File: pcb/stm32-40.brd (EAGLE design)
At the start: 69.8 x 57.1 mm, 97 parts, among them IC1 STM32F103RBT6, IC2 CAT24M01WI-GT3, IC3 MAX487-S, IC4 AMIS30663CANG2G, Q1 32768Hz, Q2 8MHz, Q3 MMBT2222, SW1 KSS-2EG4430, SW2 KSS-2EG4430, SW3 KSS-2EG4430, SW4 KSS-2EG4430, SW5 KSS-2EG4430, X1 MCV3, X2 MCV3

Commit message: ...
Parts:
- added R45, R46: 200, rc-master-smd:R0603
- R42: value 4.7K -> 200
- moved Q3 31.2 mm to (48.3, 60.3)
- moved R42 20.3 mm to (17.8, 51.4), turned to 270 degrees
- moved R44 18.2 mm to (54.6, 59.7)
- moved LCD1 1.42 mm to (39.4, 37.5)
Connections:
- removed net BL: R44.2
- net !LCD_CS: now also R46.2
- net !RESET: no longer R42.2
- net GND: no longer R42.1
- net LCD_CLK: now also R45.2
- net LCD_DATA: now also R42.2
- net PA1: now also R46.1
- net PA2: now also R42.1
- net PA4: now also R45.1
- net PD2: now also R44.2
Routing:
- net TIM3_CH4: track 46.4 -> 51.4 mm
- net TIM3_CH2: track 54.5 -> 59.4 mm
- net TIM3_CH3: track 49.1 -> 53.7 mm
- net N$44: track 12.3 -> 16.4 mm, vias 2 -> 0
- net TIM3_CH1: track 58.5 -> 62.5 mm

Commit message: pcb...
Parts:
- moved R43 53.1 mm to (40.6, 14.6), turned to 90 degrees
- moved Q3 49.6 mm to (46.4, 10.8), turned to 90 degrees
- moved R44 43.8 mm to (54.0, 15.9), turned to 90 degrees
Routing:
- net !LCD_CS: track 0.00 -> 61.5 mm
- net LCD_DATA: track 0.00 -> 60.9 mm, vias 0 -> 2
- net LCD_CLK: track 0.00 -> 59.0 mm, vias 0 -> 2
- net PD2: track 41.7 -> 79.7 mm
- net PC13: track 9.00 -> 46.0 mm
- net +3V3: track 111.0 -> 131.6 mm
- net N$32: track 0.00 -> 11.5 mm
- net N$31: track 0.00 -> 5.23 mm
- net N$29: track 0.00 -> 4.05 mm
- net SWDIO: track 46.9 -> 44.1 mm
- net BOOT0: track 48.9 -> 46.2 mm
- net SWCLK: track 49.9 -> 47.2 mm
- net !RESET: track 70.3 -> 67.7 mm
- net GND: vias 25 -> 31

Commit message: final route
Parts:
- moved G1 70.8 mm to (14.0, 15.2), turned to 270 degrees
- moved C13 55.1 mm to (39.1, 14.6), turned to 270 degrees
- moved R41 24.4 mm to (11.4, 48.3), turned to 180 degrees
- moved R2 16.6 mm to (19.1, 26.0), flipped to the top
- moved R5 3.18 mm to (5.08, 22.9)
- moved C14 2.54 mm to (8.26, 9.53)
- moved U1 2.54 mm to (8.26, 15.9)
- moved R1 1.42 mm to (1.91, 13.3), turned to 270 degrees
- moved R25 1.42 mm to (54.0, 20.3)
- moved R44 1.27 mm to (52.7, 15.9)
- moved SW5 1.27 mm to (15.9, 29.8)
- moved C19 1.27 mm to (47.0, 33.7)
- moved SW4 0.64 mm to (15.9, 37.5)
- moved C1 0.64 mm to (37.5, 18.4)
- moved C2 0.64 mm to (39.1, 18.4)
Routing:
- net +5V: track 23.7 -> 136.6 mm, vias 0 -> 4
- net +3V3: track 131.6 -> 183.5 mm, vias 5 -> 8
- net VBAT: track 5.78 -> 30.8 mm, vias 0 -> 3
- net !RESET: track 67.7 -> 89.0 mm, vias 3 -> 4
- net N$30: track 9.38 -> 29.0 mm, vias 1 -> 0
- net PC13: track 46.0 -> 64.6 mm
- net !LCD_CS: track 61.5 -> 67.9 mm
- net PA4: track 41.8 -> 46.9 mm
- net BOOT1: track 4.60 -> 9.26 mm, vias 0 -> 1
- net N$2: track 17.1 -> 20.6 mm, vias 1 -> 3
- net N$44: track 16.4 -> 13.3 mm, vias 0 -> 2
- net PA2: track 42.7 -> 45.3 mm
- net PA1: track 45.0 -> 47.4 mm
- net RXD1: track 45.9 -> 43.7 mm
- net LCD_CLK: track 59.0 -> 60.9 mm
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
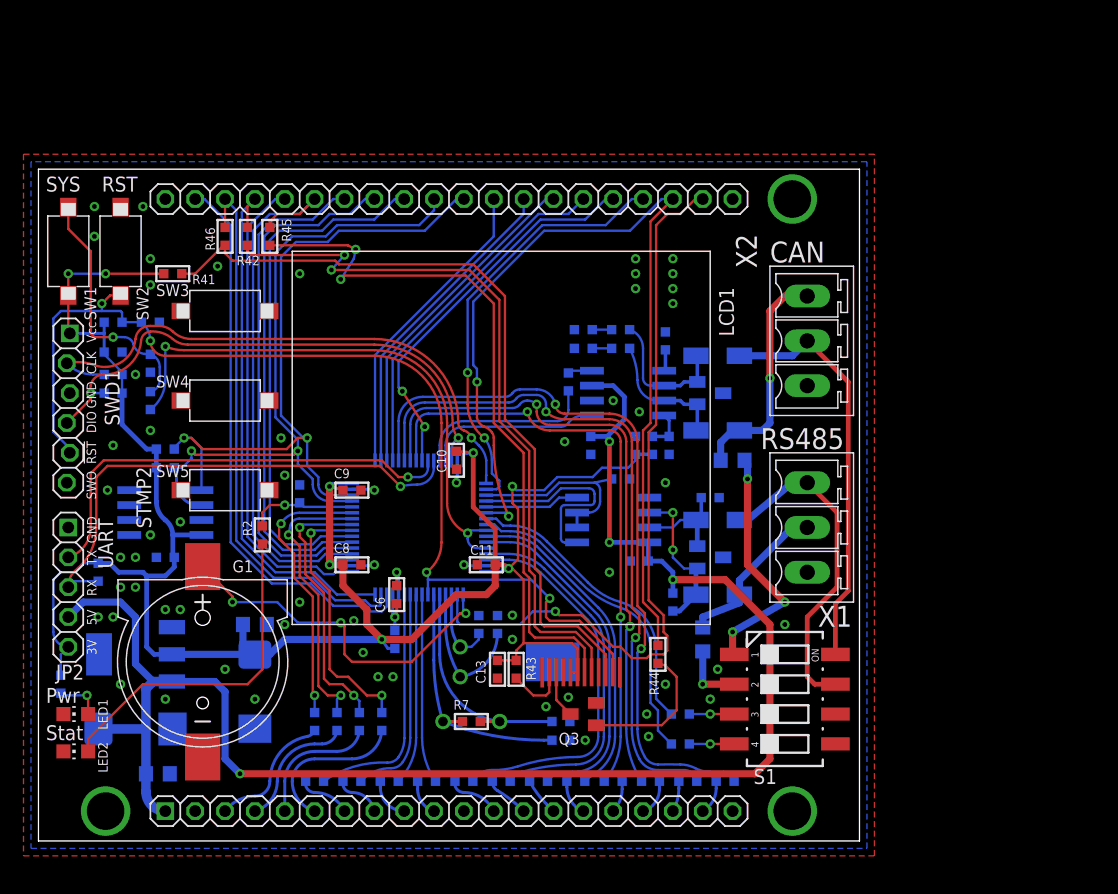
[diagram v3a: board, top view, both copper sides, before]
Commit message: 40 pin mesonine module done. Need check sch and pcb
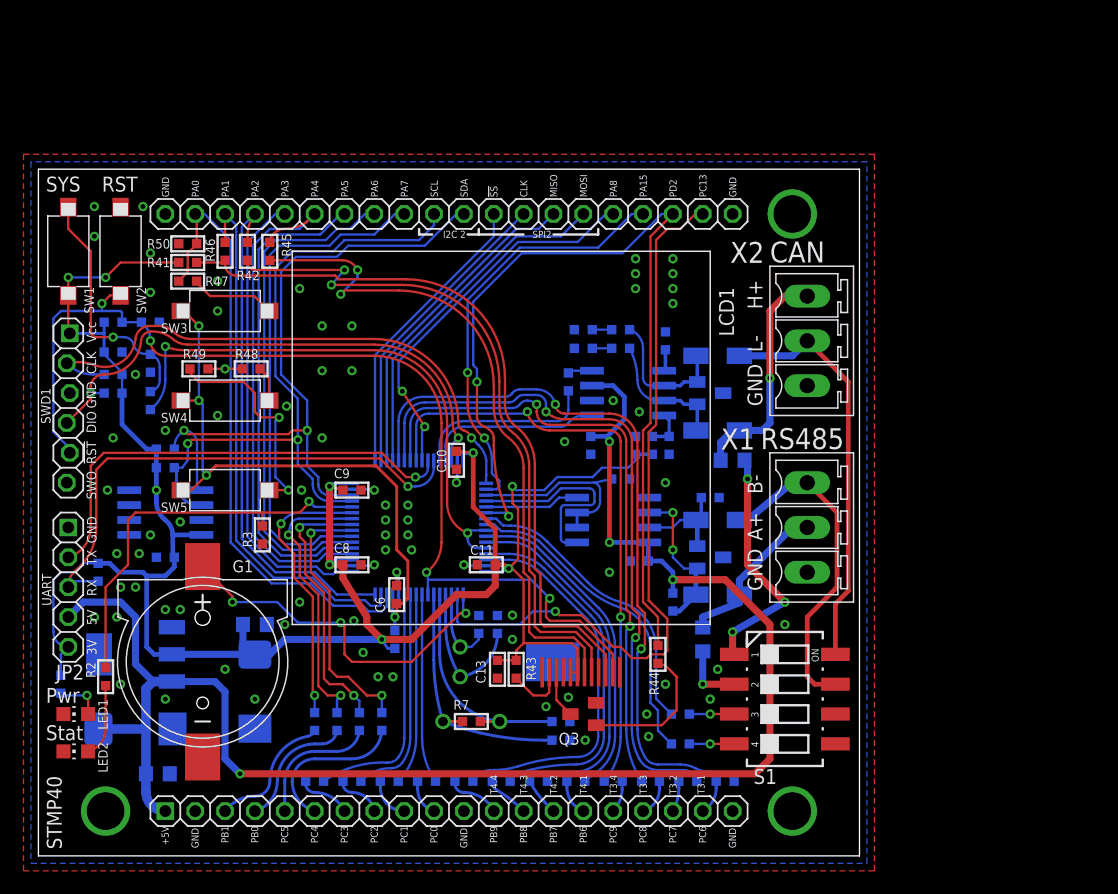
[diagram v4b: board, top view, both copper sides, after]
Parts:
- added R47, R50: 1K, rc-master-smd:R0603
- added R48: 2K, rc-master-smd:R0603
- added R49: 3.9K, rc-master-smd:R0603
- moved R2 18.0 mm to (5.71, 14.0)
- moved R3 4.72 mm to (19.1, 26.0), flipped to the top, turned to 270 degrees
- moved R41 1.59 mm to (12.7, 49.2)
- moved R42 1.27 mm to (17.8, 50.2)
- moved R45 1.27 mm to (19.7, 50.2)
- moved R46 1.27 mm to (15.9, 50.2)
- renumbered STMP2 to STMP40
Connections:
- new net N$33: R47.1, SW3.2
- new net N$34: R48.1, SW4.2
- new net N$35: R49.1, SW5.2
- net GND: now also R50.1; no longer SW3.1, SW4.1, SW5.1
- net PA0: now also R47.2, R48.2, R49.2, R50.2
- net VDDA: now also SW3.1, SW4.1, SW5.1
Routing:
- net VDDA: track 4.32 -> 51.8 mm, vias 1 -> 4
- net BOOT1: track 9.26 -> 34.5 mm
- net N$30: track 29.0 -> 6.10 mm
- net N$35: track 0.00 -> 18.9 mm, vias 0 -> 2
- net PA0: track 47.8 -> 56.3 mm, vias 0 -> 1
- net !LCD_CS: track 67.9 -> 60.6 mm
- net N$33: track 0.00 -> 7.29 mm
- net LCD_DATA: track 62.6 -> 57.4 mm
- net LCD_CLK: track 60.9 -> 55.9 mm
- net N$34: track 0.00 -> 3.02 mm
- net PA4: track 46.9 -> 45.1 mm
- net PD2: track 81.3 -> 79.5 mm
- net PA2: track 45.3 -> 43.9 mm
- net PA5: track 43.0 -> 41.7 mm
- net SPI2_SCLK: track 27.3 -> 26.0 mm
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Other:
- board size 69.8 x 57.1 mm -> 69.8 x 58.4 mm
- board text added: "!SS"
- board text added: "+5V"
- board text added: "A+"
- board text added: "B-"
- board text added: "CLK"
- board text added: "GND"
- board text added: "H+"
- board text added: "I2C 2"
- board text added: "L-"
- board text added: "MISO"
- board text added: "MOSI"
- board text added: "PA0"
- board text added: "PA1"
- board text added: "PA15"
- board text added: "PA2"
- board text added: "PA3"
- board text added: "PA4"
- board text added: "PA5"
- board text added: "PA6"
- board text added: "PA7"
- board text added: "PA8"
- board text added: "PB0"
- board text added: "PB1"
- board text added: "PB6"
- board text added: "PB7"
- board text added: "PB8"
- board text added: "PB9"
- board text added: "PC0"
- board text added: "PC1"
- board text added: "PC13"
- board text added: "PC2"
- board text added: "PC3"
- board text added: "PC4"
- board text added: "PC5"
- board text added: "PC6"
- board text added: "PC7"
- board text added: "PC8"
- board text added: "PC9"
- board text added: "PD2"
- board text added: "SCL"
- board text added: "SDA"
- board text added: "SPI2"
- board text added: "T3.1"
- board text added: "T3.2"
- board text added: "T3.3"
- board text added: "T3.4"
- board text added: "T4.1"
- board text added: "T4.2"
- board text added: "T4.3"
- board text added: "T4.4"

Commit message: stm32-40 ready to production PCB. some changes in platform
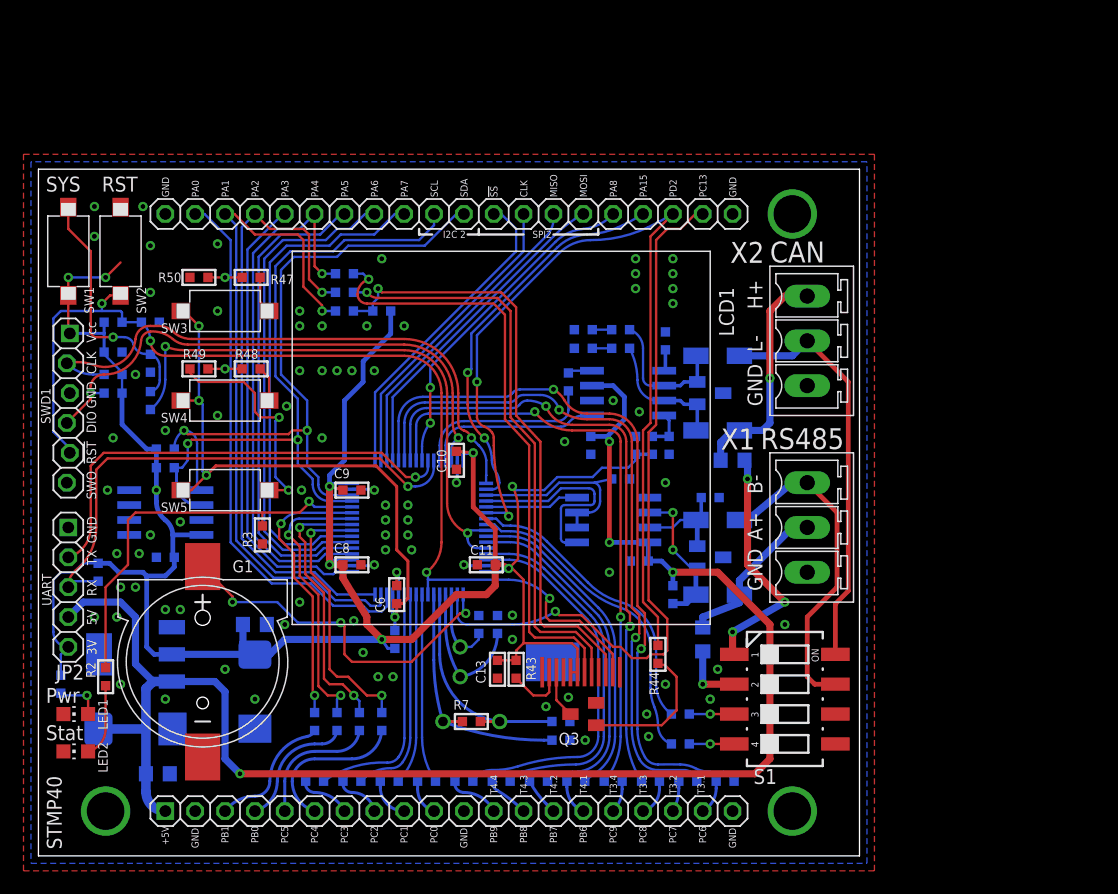
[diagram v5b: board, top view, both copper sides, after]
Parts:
- added U$1: LOGO, logo:TT_LOGO
- moved R41 17.0 mm to (29.2, 45.1), flipped to the bottom
- moved R46 11.4 mm to (26.0, 45.1), flipped to the bottom, turned to 180 degrees
- moved R42 8.96 mm to (26.0, 46.7), flipped to the bottom, turned to 180 degrees
- moved R45 6.63 mm to (26.0, 48.3), flipped to the bottom, turned to 180 degrees
- moved R47 5.41 mm to (18.1, 47.9)
- moved R50 3.01 mm to (13.7, 47.9)
- moved R25 0.63 mm to (54.0, 21.0)
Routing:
- net PA1: track 46.1 -> 59.1 mm, vias 0 -> 1
- net +3V3: track 184.7 -> 196.7 mm
- net PA2: track 43.9 -> 53.2 mm, vias 0 -> 1
- net !LCD_CS: track 60.6 -> 52.0 mm, vias 0 -> 1
- net LCD_DATA: track 57.4 -> 49.3 mm, vias 2 -> 1
- net LCD_CLK: track 55.9 -> 51.5 mm, vias 2 -> 1
- net N$33: track 7.29 -> 3.17 mm
- net PA8: track 32.6 -> 28.6 mm
- net PA0: track 56.3 -> 53.4 mm, vias 1 -> 2
- net PD2: track 79.5 -> 76.6 mm
- net PA15: track 35.8 -> 32.9 mm
- net SPI2_MOSI: track 29.9 -> 27.9 mm
- net SPI2_NSS: track 25.2 -> 27.1 mm
- net PA4: track 45.1 -> 46.7 mm, vias 0 -> 1
- net BOOT0: track 46.2 -> 47.7 mm
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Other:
- board text added: "STM32 stamp module Rev.A.14"
- board text added: "tuxotronic.org"

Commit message: some pcb fixes
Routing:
- net +3V3: track 196.7 -> 183.6 mm, vias 9 -> 7
- net !LCD_CS: track 52.0 -> 48.3 mm
- net LCD_DATA: track 49.3 -> 45.7 mm
- net LCD_CLK: track 51.5 -> 48.1 mm
- net BOOT1: track 34.5 -> 32.9 mm
- net TXD1: track 39.4 -> 38.2 mm
- net N$35: track 18.9 -> 17.8 mm
- net PA2: track 53.2 -> 52.2 mm
- net RXD1: track 44.7 -> 43.6 mm
- net N$32: track 12.2 -> 11.2 mm
- net PD2: track 76.6 -> 75.7 mm
- net PA1: track 59.1 -> 58.3 mm
- net PB0: track 24.0 -> 23.4 mm
- net PC4: track 22.7 -> 22.1 mm
- net GND: vias 82 -> 91

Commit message: little button fix
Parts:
- added R51: 330, rc-master-smd:R0603
- C1, C2: value 10pF -> 0.1
- C14, C16: value 100uF/6V3 -> 0.1; device rc-master-smd:SMC_D -> rc-master-smd:C0603
- C17: device rc-master-smd:C0805 -> rc-master-smd:C0603
- C19, C20: value 0.1 -> 560pF
- C21: value 0.1 -> 100uF/6V3; device rc-master-smd:C0603 -> rc-master-smd:SMC_D
- C22: value 560pF -> 0.1; device rc-master-smd:C0603 -> rc-master-smd:C0805
- C23: value 560pF -> 100uF/6V3; device rc-master-smd:C0603 -> rc-master-smd:SMC_D
- C3: value 22pF -> 0.1
- C4: value 22pF -> 10pF
- C5: value 0.1 -> 10pF
- C6, C7: value 0.1 -> 22pF
- IC1: value STM32F103RBT6 -> CAT24M01WI-GT3; device stm32:TQFP64 -> stm32-by-pb:SO08
- IC2: value CAT24M01WI-GT3 -> STM32F103RBT6; device stm32-by-pb:SO08 -> stm32:TQFP64
- IC3: value MAX487-S -> AMIS30663CANG2G; device rs232-rs485:SO08 -> interfaces:SO08
- IC4: value AMIS30663CANG2G -> MAX487-S; device interfaces:SO08 -> rs232-rs485:SO08
- R1, R2: value 220 -> 10K
- R10: value 10K -> 2.2K
- R11, R41: value 4.7K -> 10K
- R12: value 4.7K -> 1K
- R13, R22: value 10 -> 2K
- R14: value 10 -> 3.9K
- R15: value 10 -> 1M
- R16: value 10 -> 1K
- R17, R18, R19: value 10 -> 200
- R20: value 10 -> 4.7K
- R23: value 10 -> 10K
- R24: value 10 -> 100
- R25, R27: value 560 -> 10
- R26: value 10K -> 10
- R28, R30: value 120 -> 10; device rc-master-smd:R0805 -> rc-master-smd:R0603
- R29, R31: value 330 -> 10
- R3, R4: value 10K -> 4.7K
- R32: value 0 -> 10
- R33, R34, R35: value 100 -> 10
- R36: value NC -> 10
- R42: value 200 -> 0
- R43: value 10 -> NC
- R44: value 2K -> 560
- R45: value 200 -> 100
- R46: value 200 -> 560
- R47: value 1K -> 100
- R48: value 2K -> 120; device rc-master-smd:R0603 -> rc-master-smd:R0805
- R49: value 3.9K -> 120; device rc-master-smd:R0603 -> rc-master-smd:R0805
- R5: value 10K -> 220
- R50: value 1K -> 330
- R6: value 2.2K -> 220
- R7: value 1M -> 10K
- moved C21 55.9 mm to (8.26, 9.53), turned to 180 degrees
- moved R16 55.5 mm to (13.7, 47.9), flipped to the top
- moved R50 55.3 mm to (54.6, 10.8), flipped to the bottom
- moved R14 54.4 mm to (13.7, 40.2), flipped to the top, turned to 0 degrees
- moved R13 53.4 mm to (18.1, 40.2), flipped to the top
- moved C7 50.4 mm to (44.5, 8.57)
- moved C17 49.3 mm to (50.8, 33.7), turned to 90 degrees
- moved C3 48.7 mm to (9.53, 44.1)
- moved R18 46.2 mm to (26.0, 48.3)
- moved R49 46.1 mm to (59.1, 32.4), flipped to the bottom, turned to 180 degrees
- moved R17 46.0 mm to (26.0, 46.7)
- moved C14 45.2 mm to (51.1, 23.8), turned to 0 degrees
- moved R48 44.8 mm to (56.5, 17.1), flipped to the bottom, turned to 270 degrees
- moved R35 44.7 mm to (26.7, 5.08)
- moved R19 42.2 mm to (26.0, 45.1)
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- renumbered JP2 to JP1, STMP40 to STMP1
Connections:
- new net PB5: IC2.57, R7.1
- net !LCD_CS: now also R19.2, R20.1; no longer R41.1, R46.2
- net !RESET: now also C3.1, IC2.7, R11.1, SW1.2; no longer C5.1, IC1.7, R8.1, SW2.2
- net +3V3: now also C1.1, C17.1, C2.1, C22.1, C23.+, IC1.8, IC2.19, IC2.32, IC2.48, IC2.64, R1.2, R2.2, R20.2, R21.2, R23.2, R3.2, R4.2, R42.1, R5.1, SW2.2; no longer C11.1, C15.1, C16.+, C20.1, C7.1, IC1.19, IC1.32, IC1.48, IC1.64, IC2.8, R1.1, R10.2, R12.2, R32.1, R41.2, R43.2, R5.2, R8.2, R9.2, SW1.2
- net +5V: now also C14.1, C15.1, C16.1, C21.+, IC3.3, IC4.8, R46.2; no longer C14.+, C17.1, C18.1, C19.1, IC3.8, IC4.3, R25.2
- net BOOT0: now also IC2.60, R8.1; no longer IC1.57, IC1.60, R4.1
- net BOOT1: now also IC2.28, R6.1, R9.1; no longer IC1.28, R2.1, R3.1
- net CAN_CTRL: now also IC3.8, R42.2, R43.2; no longer IC4.8, R32.2, R36.2
- net CAN_H: now also R49.1; no longer R30.1
- net CAN_RX: now also IC2.44, R24.1; no longer IC1.44, R33.1
- net CAN_TX: now also IC2.45, IC3.1; no longer IC1.45, IC4.1
- net DE3: now also IC2.53, IC4.4; no longer IC1.53, IC3.4
- net GND: now also C14.2, C16.2, C21.-, C23.-, IC1.1, IC1.2, IC1.3, IC1.4, IC1.7, IC2.12, IC2.18, IC2.31, IC2.47, IC2.63, IC3.2, IC4.5, R10.1, R16.1, R41.1, R43.1, R44.1, R9.2, SW1.1; no longer C14.-, C16.-, C21.2, C23.2, IC1.12, IC1.18, IC1.31, IC1.47, IC1.63, IC2.1, IC2.2, IC2.3, IC2.4, IC2.7, IC3.5, IC4.2, R26.1, R27.1, R3.2, R36.1, R50.1, R6.1, SW2.1
- net LCD_CLK: now also R18.2; no longer R45.2
- net LCD_DATA: now also R17.2; no longer R42.2
- net N$1: now also C18.1, IC3.5; no longer C21.1, IC4.5
- net N$10: now also R51.1; no longer R31.1
- net N$11: now also R33.1; no longer R21.1
- net N$13: now also R5.2; no longer R1.2
- net N$14: now also R34.1; no longer R22.1
- net N$15: now also R25.1; no longer R13.1
- net N$16: now also R26.1; no longer R14.1
- net N$17: now also R27.1; no longer R15.1
- net N$18: now also R28.1; no longer R16.1
- net N$19: now also R29.1; no longer R17.1
- net N$2: now also R49.2; no longer R30.2
- net N$20: now also R30.1; no longer R18.1
- net N$21: now also R31.1; no longer R19.1
- net N$22: now also R32.1; no longer R20.1
- net N$23: now also R35.1; no longer R23.1
- net N$24: now also R36.1; no longer R24.1
- net N$3: now also R10.2, R7.2, R8.2, SW2.1; no longer R4.2, R6.2, SW1.1
- net N$30: now also R6.2; no longer R2.2
- net N$31: now also R21.1; no longer R43.1
- net N$32: now also R22.1; no longer R44.1
- net N$33: now also R12.1; no longer R47.1
- net N$34: now also R13.1; no longer R48.1
- net N$35: now also R14.1; no longer R49.1
- net N$44: now also IC4.6, R46.1; no longer IC3.6, R25.1
- net N$51: now also IC3.7, R45.2; no longer IC4.7, R34.2
- net N$52: now also IC3.6, R47.2; no longer IC4.6, R35.2
- net N$54: now also C20.1, R47.1; no longer C23.1, R35.1
- net N$55: now also C19.1, R45.1; no longer C22.1, R34.1
- net N$6: now also IC4.7, R44.2; no longer IC3.7, R27.2
- net N$7: now also IC3.4, R24.2; no longer IC4.4, R33.2
- net N$8: now also R48.2; no longer R28.2
- net N$9: now also R50.1; no longer R29.1
- net OSC32_IN: now also C4.1, IC2.3; no longer C1.1, IC1.3
- net OSC32_OUT: now also C5.1, IC2.4; no longer C2.1, IC1.4
- net OSC_IN: now also C6.1, IC2.5, R15.2; no longer C3.1, IC1.5, R7.2
- net OSC_OUT: now also C7.1, IC2.6, R15.1; no longer C4.1, IC1.6, R7.1
- net PA0: now also IC2.14, R12.2, R13.2, R14.2, R16.2; no longer IC1.14, R47.2, R48.2, R49.2, R50.2
- net PA1: now also IC2.15, R19.1; no longer IC1.15, R46.1
- net PA15: now also IC2.50; no longer IC1.50
- net PA2: now also IC2.16, R17.1; no longer IC1.16, R42.1
- net PA3: now also IC2.17; no longer IC1.17
- net PA4: now also IC2.20, R18.1; no longer IC1.20, R45.1
- net PA5: now also IC2.21; no longer IC1.21
- net PA6: now also IC2.22; no longer IC1.22
- net PA7: now also IC2.23; no longer IC1.23
- net PA8: now also IC2.41; no longer IC1.41
- net PB0: now also IC2.26; no longer IC1.26
- net PB1: now also IC2.27; no longer IC1.27
- net PC0: now also IC2.8, R33.2; no longer IC1.8, R21.2
- net PC1: now also IC2.9, R34.2; no longer IC1.9, R22.2
- net PC13: now also IC2.2; no longer IC1.2
- net PC2: now also IC2.10, R35.2; no longer IC1.10, R23.2
- net PC3: now also IC2.11, R36.2; no longer IC1.11, R24.2
- net PC4: now also IC2.24; no longer IC1.24
- net PC5: now also IC2.25; no longer IC1.25
- net PD2: now also IC2.54, R22.2; no longer IC1.54, R44.2
- net RS485_A: now also R48.1; no longer R28.1
- net RXD1: now also IC2.43, R23.1; no longer IC1.43, R5.1
- net RXD3: now also IC2.52, IC4.1; no longer IC1.52, IC3.1
- net SCL2: now also IC1.6, IC2.29, R3.1; no longer IC1.29, IC2.6, R11.1
- net SDA2: now also IC1.5, IC2.30, R4.1; no longer IC1.30, IC2.5, R12.1
- net SPI2_MISO: now also IC2.35; no longer IC1.35
- net SPI2_MOSI: now also IC2.36; no longer IC1.36
- net SPI2_NSS: now also IC2.33; no longer IC1.33
- net SPI2_SCLK: now also IC2.34; no longer IC1.34
- net SW3: now also IC2.55, R50.2; no longer IC1.55, R29.2
- net SW4: now also IC2.56, R51.2; no longer IC1.56, R31.2
- net SWCLK: now also IC2.49, R1.1; no longer IC1.49, R9.1
- net SWDIO: now also IC2.46, R2.1; no longer IC1.46, R10.1
- net TIM3_CH1: now also IC2.37, R25.2; no longer IC1.37, R13.2
- net TIM3_CH2: now also IC2.38, R26.2; no longer IC1.38, R14.2
- net TIM3_CH3: now also IC2.39, R27.2; no longer IC1.39, R15.2
- net TIM3_CH4: now also IC2.40, R28.2; no longer IC1.40, R16.2
- net TIM4_CH1: now also IC2.58, R29.2; no longer IC1.58, R17.2
- net TIM4_CH2: now also IC2.59, R30.2; no longer IC1.59, R18.2
- net TIM4_CH3: now also IC2.61, R31.2; no longer IC1.61, R19.2
- net TIM4_CH4: now also IC2.62, R32.2; no longer IC1.62, R20.2
- net TXD1: now also IC2.42; no longer IC1.42
- net TXD3: now also IC2.51, IC4.2, IC4.3, R41.2; no longer IC1.51, IC3.2, IC3.3, R26.2
- net VBAT: now also IC2.1; no longer IC1.1
- net VDDA: now also C11.1, IC2.13; no longer C6.1, IC1.13
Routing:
- net BOOT0: track 47.7 -> 4.50 mm, vias 2 -> 1
- net N$3: track 21.1 -> 55.6 mm, vias 1 -> 2
- net PB5: track 0.00 -> 2.87 mm, vias 0 -> 1
- net VDDA: track 51.4 -> 50.2 mm
- net LCD_CLK: track 48.1 -> 47.1 mm
- net LCD_DATA: track 45.7 -> 45.0 mm
- net !LCD_CS: track 48.3 -> 47.7 mm
